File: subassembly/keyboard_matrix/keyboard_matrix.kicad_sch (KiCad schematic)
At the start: 23 parts, among them J10 Data, J11 Debug, Q101 2N7002, U1 ATSAMD10D13A-M

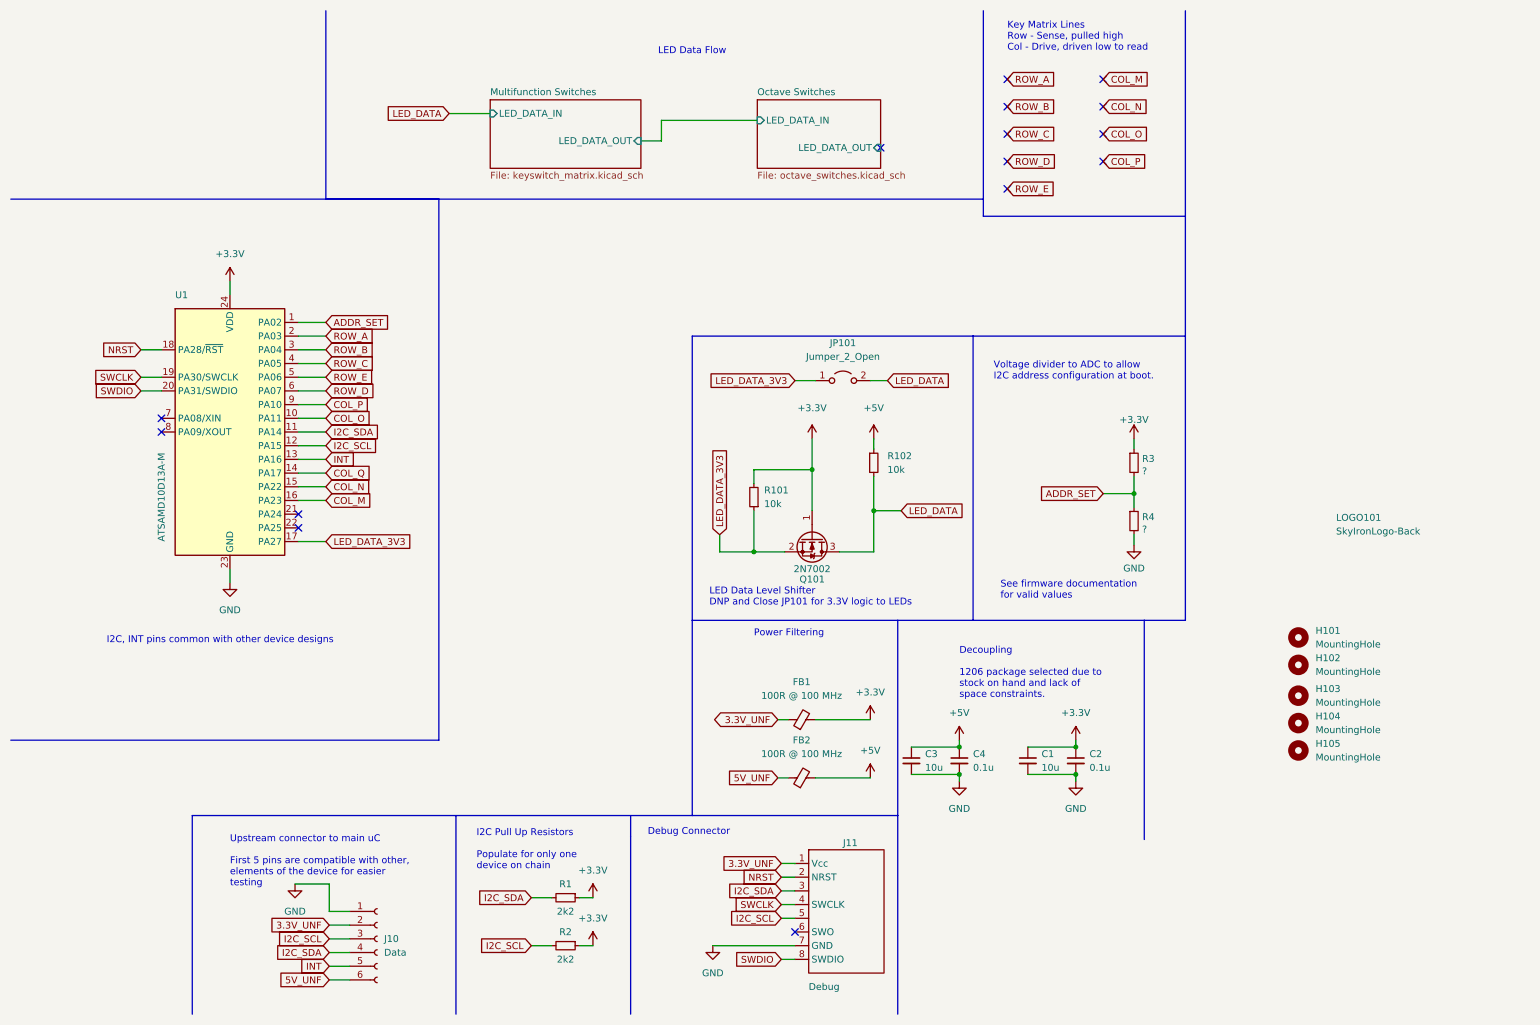
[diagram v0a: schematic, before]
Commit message: First run of keyboard board and move prototype board to rotary_encoder_board
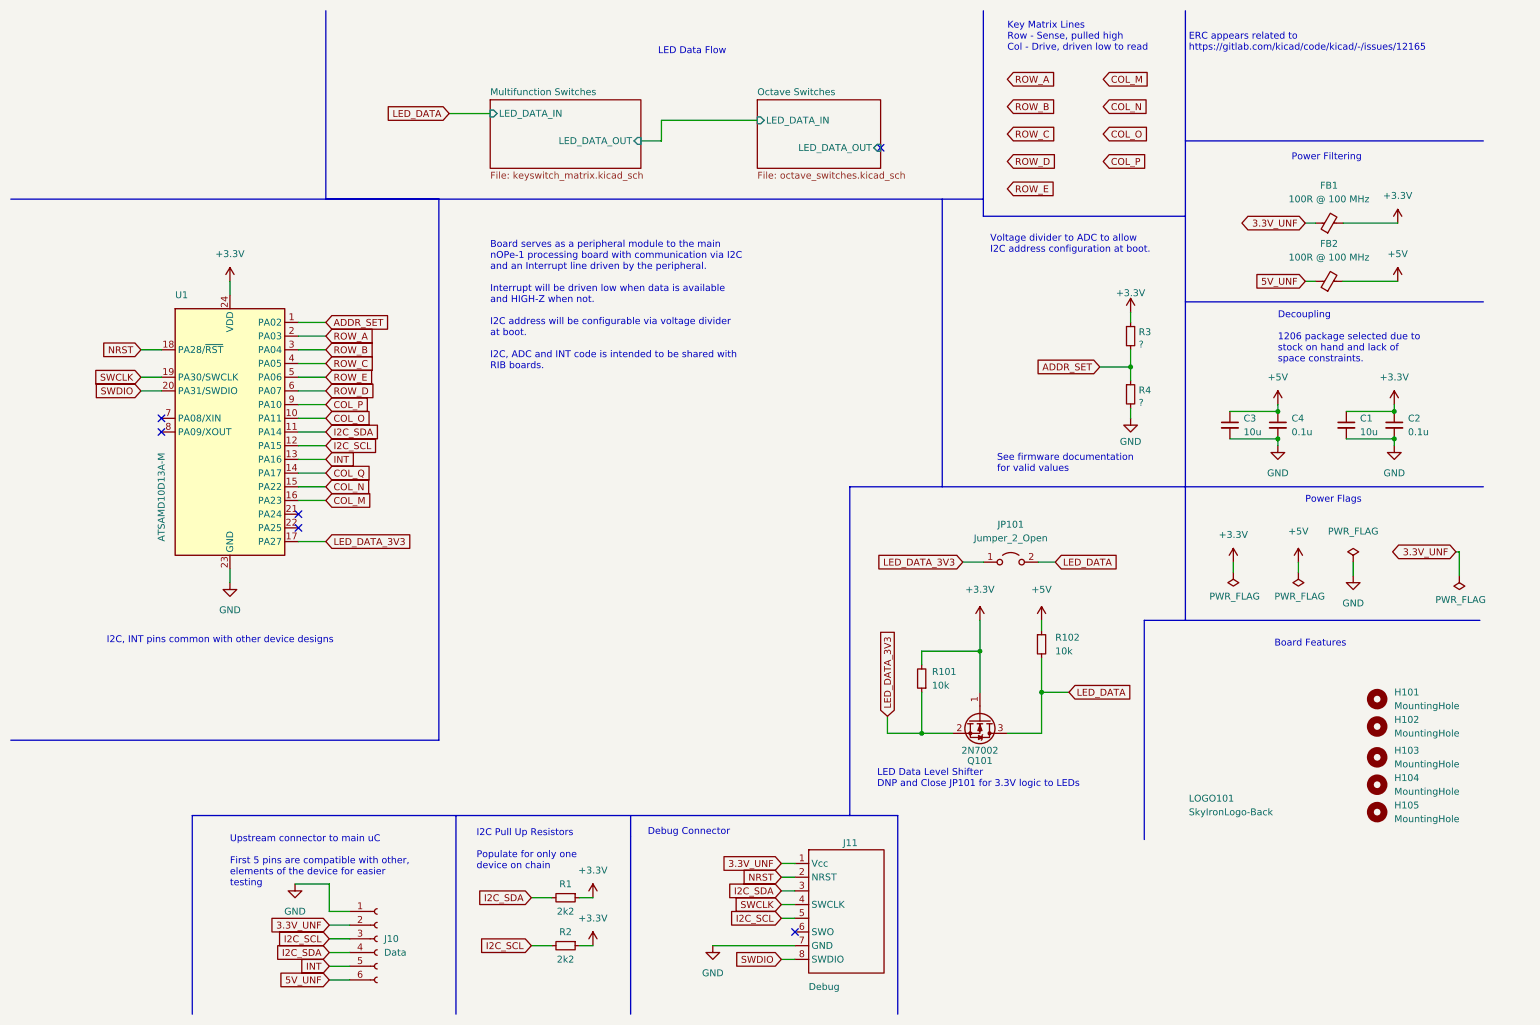
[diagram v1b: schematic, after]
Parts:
- J10: footprint Connector_PinHeader_2.54mm:PinHeader_1x06_P2.54mm_Horizontal -> Connector_PinHeader_2.54mm:PinHeader_1x06_P2.54mm_Vertical
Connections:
- no-connect marks 15 -> 6
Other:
- note added: "Board Features"
- note added: "Board serves as a peripheral module to the main nOPe-1 processing board with communication via I2C and an Interrupt line driven by the peripheral. Interrupt will be driven low when data is available and HIGH-Z when not. I2C address will be configurable via voltage divider at boot. I2C, ADC and INT code is intended to be shared with RIB boards."
- note added: "ERC appears related to https://gitlab.com/kicad/code/kicad/-/issues/12165"
- note added: "Power Flags"
- moved on the sheet: C1, C2, C3, C4, FB1, FB2, H101, H102, H103, H104, H105, JP101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
